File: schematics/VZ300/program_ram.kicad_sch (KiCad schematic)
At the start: 28 parts, among them Q2 NA31X, Q3 1502C, T1 10T, T1 50T, U1 4116, U2 4116, U3 4116, U4 4116, U5 4116, U6 4116, U7 4116, U8 4116

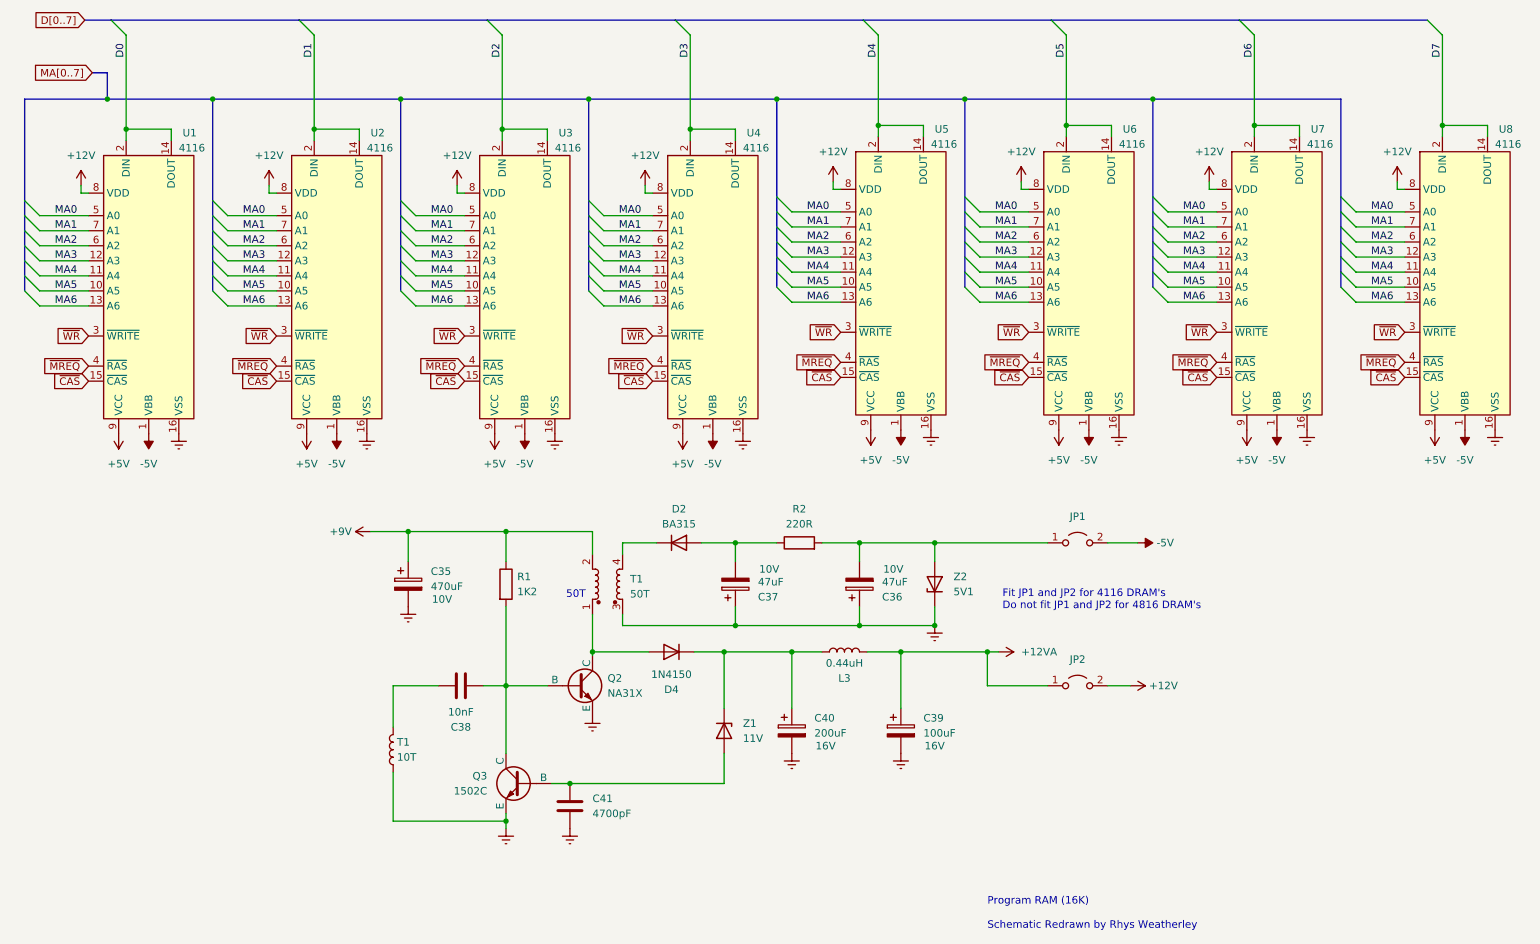
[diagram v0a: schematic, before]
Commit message: Document the placement of DRAM chips in the VZ300 schematic
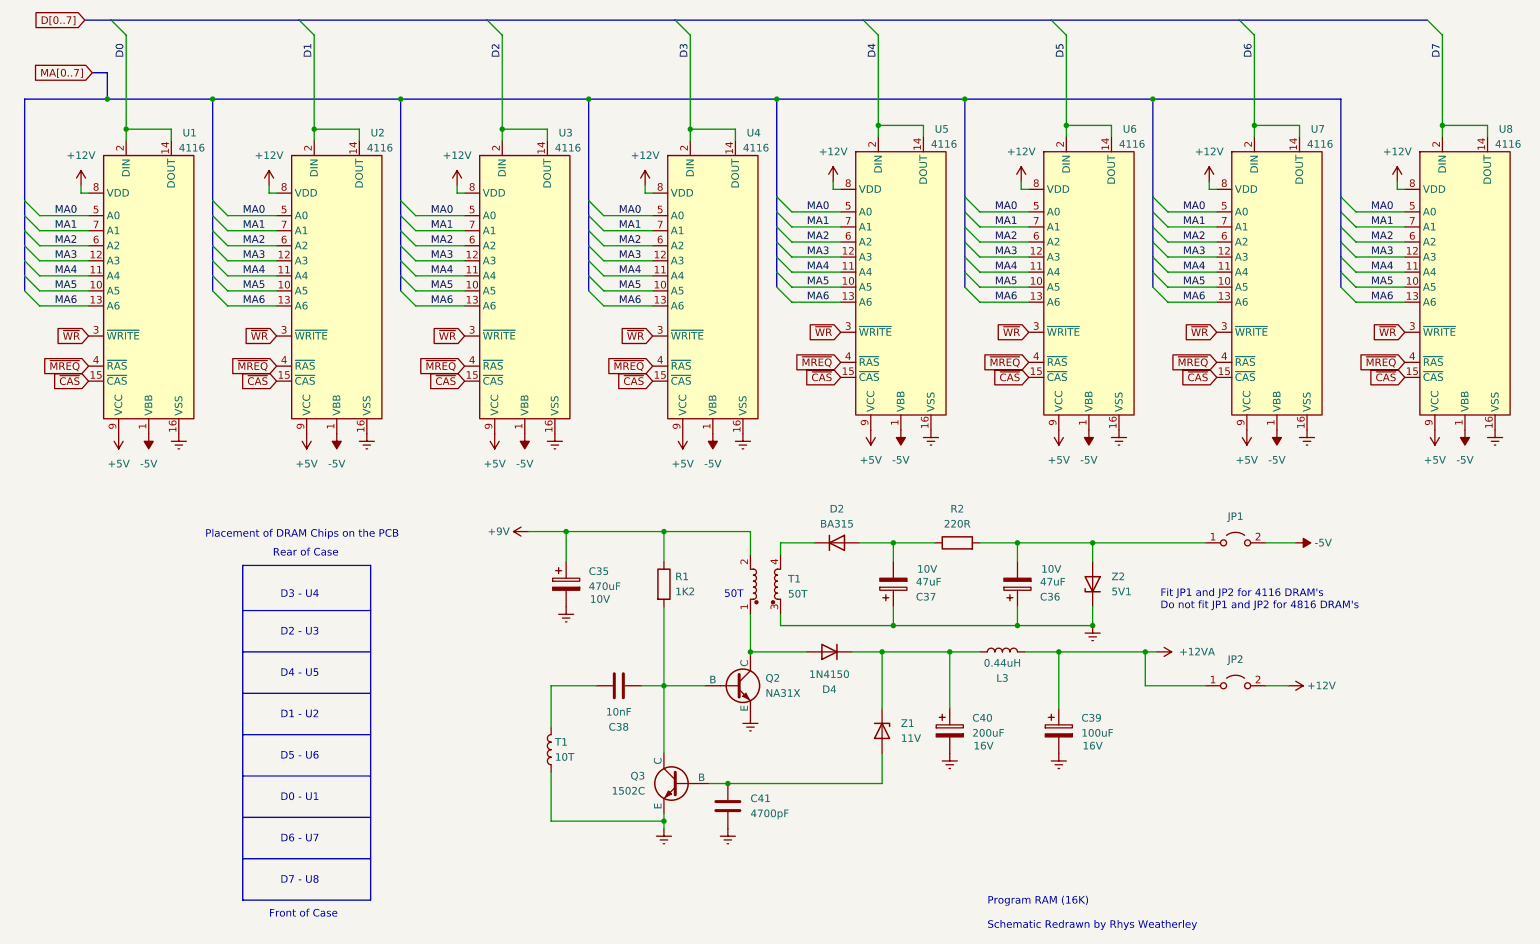
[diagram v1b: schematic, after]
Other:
- note added: "D0 - U1"
- note added: "D1 - U2"
- note added: "D2 - U3"
- note added: "D3 - U4"
- note added: "D4 - U5"
- note added: "D5 - U6"
- note added: "D6 - U7"
- note added: "D7 - U8"
- note added: "Front of Case"
- note added: "Placement of DRAM Chips on the PCB"
- note added: "Rear of Case"
- moved on the sheet: C35, C36, C37, C38, C39, C40, C41, D2, D4, JP1, JP2, L3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
